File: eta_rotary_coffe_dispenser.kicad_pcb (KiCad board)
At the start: 2 copper layers, 81 x 52 mm, 54 parts, among them J1 Conn_01x08, J3 AVR-ISP-6, J4 Conn_01x02, J5 Conn_01x04, J6 Conn_01x02, J7 Conn_01x02, Q1 IRF640NPbF, Q2 IRF640NPbF, Q3 CPH3350-TL-W, SW1 SW_Push, U1 ATmega328P-A, U2 L7805, Y1 Crystal

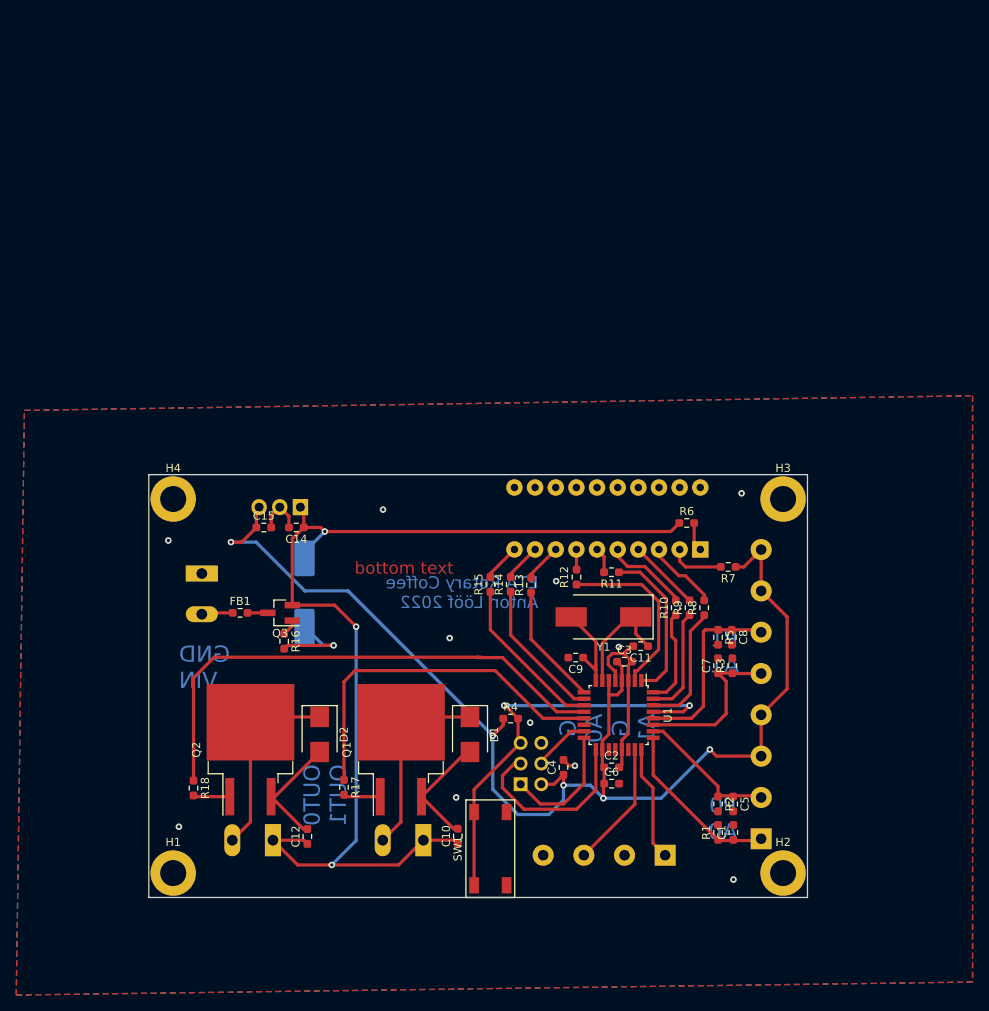
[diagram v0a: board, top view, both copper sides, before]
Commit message: start rev 2 op project with can and weight sens
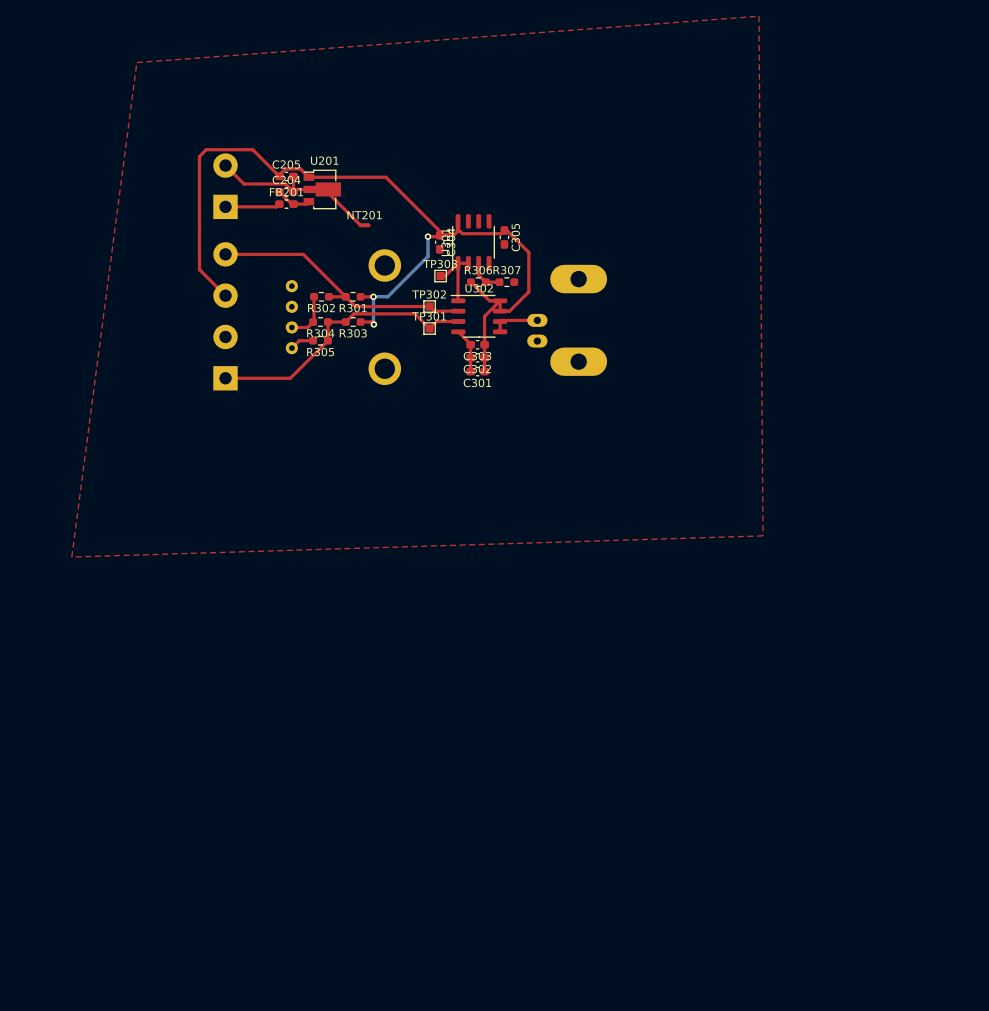
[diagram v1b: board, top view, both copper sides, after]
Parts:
- removed BAR1: HLCP-J100_2, Display:HLCP-J100
- removed C1, C14, C15, C2, C3, C4, C5, C7, C8: 100n, Resistor_SMD:R_0603_1608Metric_Pad0.98x0.95mm_HandSolder
- removed C10, C12, C6: 1u, Resistor_SMD:R_0603_1608Metric_Pad0.98x0.95mm_HandSolder
- removed C11, C9: 12p, Resistor_SMD:R_0603_1608Metric_Pad0.98x0.95mm_HandSolder
- removed C13: 470u, Capacitor_SMD:CP_Elec_10x10.5
- removed D1, D2: SM6T30A, Diode_SMD:D_SMB
- removed FB1: FerriteBead_Small, Resistor_SMD:R_0603_1608Metric_Pad0.98x0.95mm_HandSolder
- removed H1, H2, H3, H4: MountingHole_Pad, MountingHole:MountingHole_3.2mm_M3_DIN965_Pad
- removed J1: Conn_01x08, TerminalBlock_Phoenix:TerminalBlock_Phoenix_MKDS-1,5-8-5.08_1x08_P5.08mm_Horizontal
- removed J3: AVR-ISP-6, Connector_PinHeader_2.54mm:PinHeader_2x03_P2.54mm_Vertical
- removed J4, J6, J7: Conn_01x02, TerminalBlock:TerminalBlock_Altech_AK300-2_P5.00mm
- removed J5: Conn_01x04, TerminalBlock_Phoenix:TerminalBlock_Phoenix_MKDS-1,5-4_1x04_P5.00mm_Horizontal
- removed Q1, Q2: IRF640NPbF, Package_TO_SOT_SMD:TO-263-2
- removed Q3: CPH3350-TL-W, Package_TO_SOT_SMD:SOT-23_Handsoldering
- removed R1, R16, R2, R3, R4, R5: 10k, Resistor_SMD:R_0603_1608Metric_Pad0.98x0.95mm_HandSolder
- removed R10, R11, R12, R13, R14, R15, R17, R18, R7, R8, R9: 470, Resistor_SMD:R_0603_1608Metric_Pad0.98x0.95mm_HandSolder
- removed R6: 4k7, Resistor_SMD:R_0603_1608Metric_Pad0.98x0.95mm_HandSolder
- removed SW1: SW_Push, good_things:push_sw_purple
- removed U1: ATmega328P-A, Package_QFP:TQFP-32_7x7mm_P0.8mm
- removed U2: L7805, Package_TO_SOT_THT:TO-220-3_Vertical
- removed Y1: Crystal, Crystal:Crystal_SMD_EuroQuartz_MQ2-2Pin_7.0x5.0mm_HandSoldering
- added C204: 100n, Capacitor_SMD:C_0603_1608Metric_Pad1.08x0.95mm_HandSolder, F.Cu at (192.8, 57.4)
- added C205: 100n, Capacitor_SMD:C_0603_1608Metric_Pad1.08x0.95mm_HandSolder, F.Cu at (192.8, 55.5)
- added C301: 1u, Capacitor_SMD:C_0603_1608Metric_Pad1.08x0.95mm_HandSolder, F.Cu at (216.3, 79.5)
- added C302: 100n, Capacitor_SMD:C_0603_1608Metric_Pad1.08x0.95mm_HandSolder, F.Cu at (216.3, 77.8)
- added C303: 10n, Capacitor_SMD:C_0603_1608Metric_Pad1.08x0.95mm_HandSolder, F.Cu at (216.3, 76.2)
- added C304: 1u, Capacitor_SMD:C_0603_1608Metric_Pad1.08x0.95mm_HandSolder, F.Cu at (211.7, 63.6)
- added C305: 100n, Capacitor_SMD:C_0603_1608Metric_Pad1.08x0.95mm_HandSolder, F.Cu at (219.6, 63.0)
- added FB201: FerriteBead, Inductor_SMD:L_0603_1608Metric_Pad1.05x0.95mm_HandSolder, F.Cu at (192.8, 58.9)
- added J201: Conn_01x02, TerminalBlock:TerminalBlock_bornier-2_P5.08mm, B.Cu at (185.3, 59.2)
- added J301: Conn_01x04, TerminalBlock:TerminalBlock_bornier-4_P5.08mm, B.Cu at (185.3, 80.3)
- added J302: Conn_Coaxial, Connector_Coaxial:BNC_Amphenol_B6252HB-NPP3G-50_Horizontal, B.Cu at (223.7, 73.2)
- added NT201: NetTie_2, NetTie:NetTie-2_SMD_Pad0.5mm, F.Cu at (202.4, 61.5)
- added R301: 10k, Resistor_SMD:R_0603_1608Metric_Pad0.98x0.95mm_HandSolder, F.Cu at (201.0, 70.3)
- added R302: 10k, Resistor_SMD:R_0603_1608Metric_Pad0.98x0.95mm_HandSolder, F.Cu at (197.1, 70.3)
- added R303: 10k, Resistor_SMD:R_0603_1608Metric_Pad0.98x0.95mm_HandSolder, F.Cu at (201.0, 73.4)
- added R304: 10k, Resistor_SMD:R_0603_1608Metric_Pad0.98x0.95mm_HandSolder, F.Cu at (197.0, 73.4)
- added R305: 82k, Resistor_SMD:R_0603_1608Metric_Pad0.98x0.95mm_HandSolder, F.Cu at (197.0, 75.7)
- added R306: 10k, Resistor_SMD:R_0603_1608Metric_Pad0.98x0.95mm_HandSolder, F.Cu at (216.4, 68.5)
- added R307: 10k, Resistor_SMD:R_0603_1608Metric_Pad0.98x0.95mm_HandSolder, F.Cu at (219.9, 68.5)
- added RV301: 10k, good_things:B10K_POT_ETA, B.Cu at (197.3, 72.8)
- added TP301: TestPoint, TestPoint:TestPoint_Pad_1.0x1.0mm, F.Cu at (210.4, 74.2)
- added TP302: TestPoint, TestPoint:TestPoint_Pad_1.0x1.0mm, F.Cu at (210.4, 71.5)
- added TP303: TestPoint, TestPoint:TestPoint_Pad_1.0x1.0mm, F.Cu at (211.8, 67.8)
- added U201: L78L33_SOT89, Package_TO_SOT_SMD:SOT-89-3, F.Cu at (197.2, 57.1)
- added U301: LM358, Package_SO:SO-8_3.9x4.9mm_P1.27mm, F.Cu at (215.8, 63.6)
- added U302: MAX4196, Package_SO:SO-8_3.9x4.9mm_P1.27mm, F.Cu at (216.5, 72.7)
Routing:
- net VCC: track 155.2 -> 0.00 mm, vias 5 -> 0
- net +12V: track 133.3 -> 0.00 mm, vias 3 -> 0
- net +3.3VA: track 0.00 -> 112.3 mm, vias 0 -> 3
- net /ext_ctrl0: track 65.0 -> 0.00 mm
- net /isp_rst_n: track 53.0 -> 0.00 mm, vias 2 -> 0
- net GND: track 69.1 -> 21.8 mm, vias 12 -> 0
- net /ext_ctrl1: track 44.6 -> 0.00 mm
- net /scale_amp/inp: track 0.00 -> 34.4 mm
- net /scale_amp/inn: track 0.00 -> 33.6 mm
- net /ext_out1: track 24.2 -> 0.00 mm
- net /ext_out0: track 24.2 -> 0.00 mm
- net /rotary1_pulse: track 23.3 -> 0.00 mm
- net /isp_sck: track 22.8 -> 0.00 mm
- net /led_6: track 22.1 -> 0.00 mm
- net /rotary0_active: track 21.3 -> 0.00 mm
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- added copper zone on F.Cu, net GNDA
- removed copper zone on B.Cu, net GND
- removed copper zone on F.Cu, net GND
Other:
- board outline removed
- board text removed: "ETA Rotary Coffee Anton Lööf 2022"
- board text removed: "G A0 G A1"
- board text removed: "GND VIN"
- board text removed: "OUT0 OUT1"
- board text removed: "P0 A0"
- board text removed: "P1 A1"
- board text removed: "bottom text"

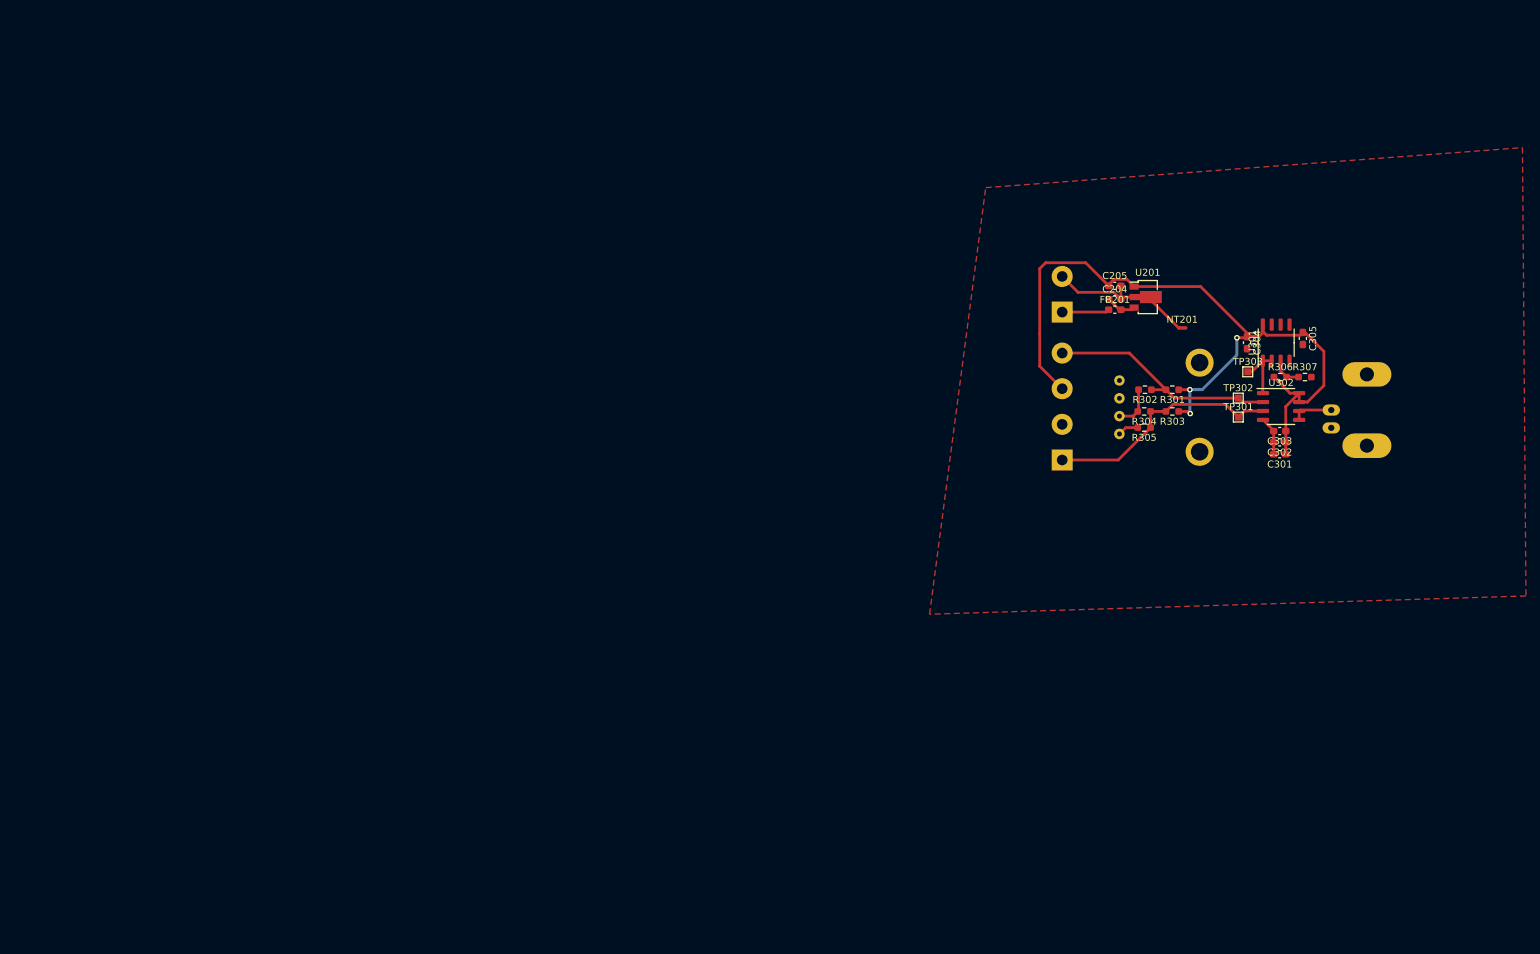
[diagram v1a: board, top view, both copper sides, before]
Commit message: some form of schematic done, still lots to test
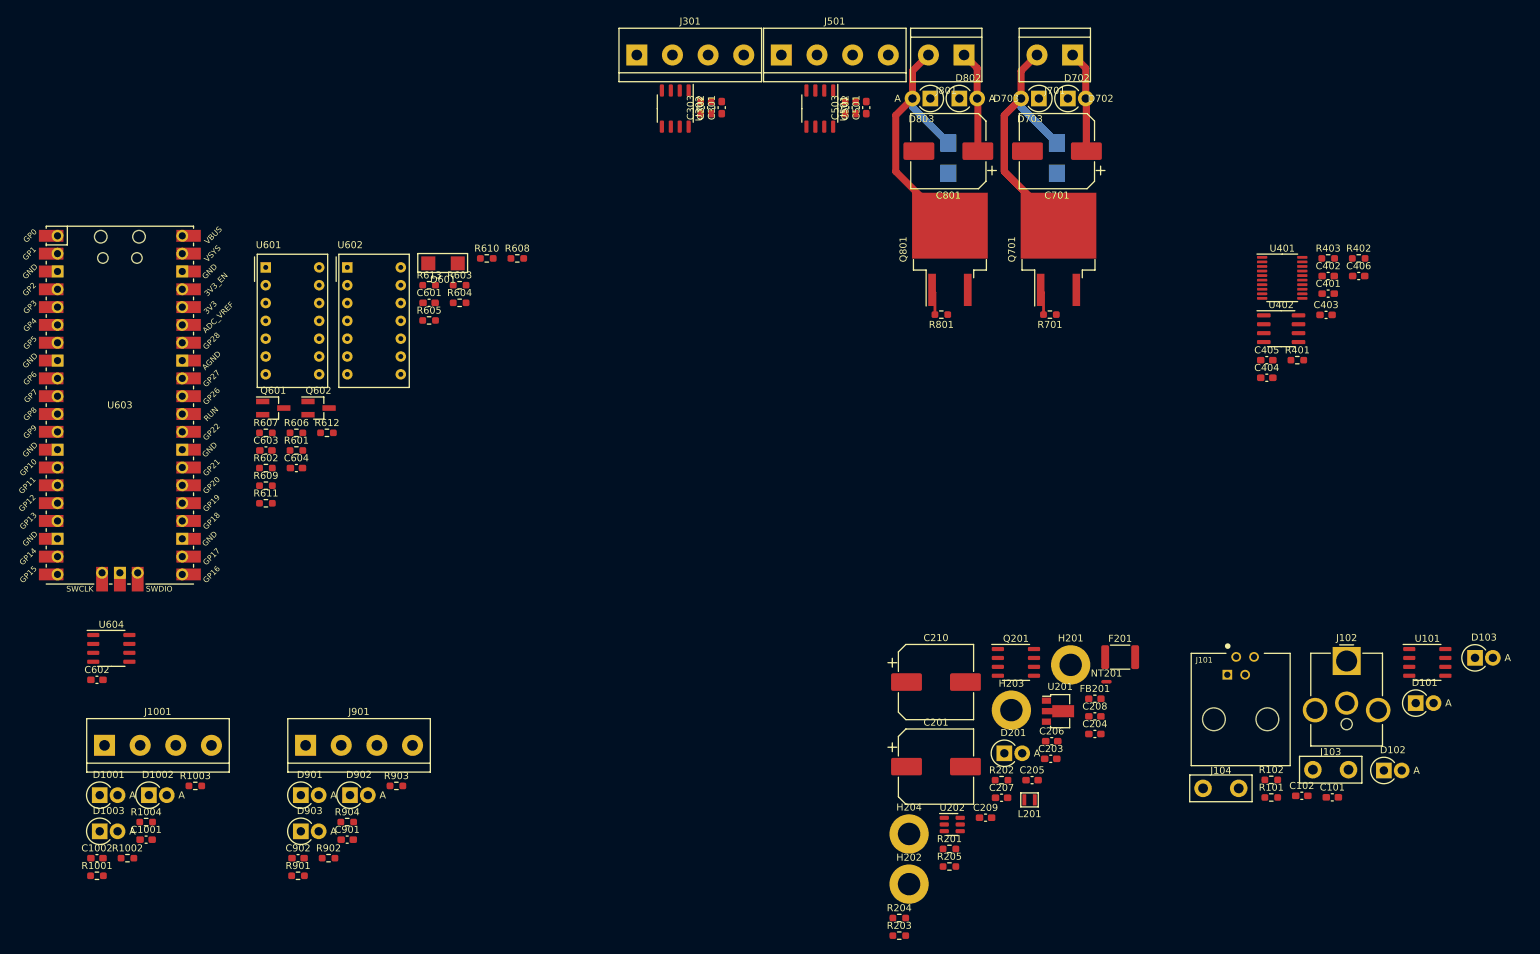
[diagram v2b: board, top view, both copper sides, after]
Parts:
- removed C304: 1u, Capacitor_SMD:C_0603_1608Metric_Pad1.08x0.95mm_HandSolder
- removed C305: 100n, Capacitor_SMD:C_0603_1608Metric_Pad1.08x0.95mm_HandSolder
- removed J201: Conn_01x02, TerminalBlock:TerminalBlock_bornier-2_P5.08mm
- removed J302: Conn_Coaxial, Connector_Coaxial:BNC_Amphenol_B6252HB-NPP3G-50_Horizontal
- removed R301, R302, R303, R304, R306, R307: 10k, Resistor_SMD:R_0603_1608Metric_Pad0.98x0.95mm_HandSolder
- removed R305: 82k, Resistor_SMD:R_0603_1608Metric_Pad0.98x0.95mm_HandSolder
- removed RV301: 10k, good_things:B10K_POT_ETA
- removed TP301, TP302, TP303: TestPoint, TestPoint:TestPoint_Pad_1.0x1.0mm
- removed U301: LM358, Package_SO:SO-8_3.9x4.9mm_P1.27mm
- added C1001: 100n, Capacitor_SMD:C_0603_1608Metric_Pad1.08x0.95mm_HandSolder, F.Cu at (54.7, 134.4)
- added C1002: 100n, Capacitor_SMD:C_0603_1608Metric_Pad1.08x0.95mm_HandSolder, F.Cu at (47.7, 137.1)
- added C101: 1u, Capacitor_SMD:C_0603_1608Metric_Pad1.08x0.95mm_HandSolder, F.Cu at (223.8, 128.4)
- added C102: 100n, Capacitor_SMD:C_0603_1608Metric_Pad1.08x0.95mm_HandSolder, F.Cu at (219.4, 128.2)
- added C201: 470u, Capacitor_SMD:CP_Elec_10x10.5, F.Cu at (167.3, 124.0)
- added C203: 1u 25V, Capacitor_SMD:C_0603_1608Metric_Pad1.08x0.95mm_HandSolder, F.Cu at (183.7, 122.9)
- added C206: 100n, Capacitor_SMD:C_0603_1608Metric_Pad1.08x0.95mm_HandSolder, F.Cu at (183.8, 120.4)
- added C207: dni, Capacitor_SMD:C_0603_1608Metric_Pad1.08x0.95mm_HandSolder, F.Cu at (176.7, 128.5)
- added C208: 22u, Capacitor_SMD:C_0603_1608Metric_Pad1.08x0.95mm_HandSolder, F.Cu at (190.0, 116.9)
- added C209: 22u, Capacitor_SMD:C_0603_1608Metric_Pad1.08x0.95mm_HandSolder, F.Cu at (174.4, 131.3)
- added C210: 470u, Capacitor_SMD:CP_Elec_10x10.5, F.Cu at (167.3, 112.0)
- added C401: 1u, Capacitor_SMD:C_0603_1608Metric_Pad1.08x0.95mm_HandSolder, F.Cu at (223.2, 56.6)
- added C402: 100n, Capacitor_SMD:C_0603_1608Metric_Pad1.08x0.95mm_HandSolder, F.Cu at (223.2, 54.1)
- added C403: 100n, Capacitor_SMD:C_0603_1608Metric_Pad1.08x0.95mm_HandSolder, F.Cu at (222.9, 59.6)
- added C404: 100n, Capacitor_SMD:C_0603_1608Metric_Pad1.08x0.95mm_HandSolder, F.Cu at (214.5, 68.6)
- added C405: 1u, Capacitor_SMD:C_0603_1608Metric_Pad1.08x0.95mm_HandSolder, F.Cu at (214.5, 66.1)
- added C406: 100n, Capacitor_SMD:C_0603_1608Metric_Pad1.08x0.95mm_HandSolder, F.Cu at (227.6, 54.1)
- added C501: 1u, Capacitor_SMD:C_0603_1608Metric_Pad1.08x0.95mm_HandSolder, F.Cu at (157.4, 30.1)
- added C502: 100n, Capacitor_SMD:C_0603_1608Metric_Pad1.08x0.95mm_HandSolder, F.Cu at (155.9, 30.1)
- added C503: 10n, Capacitor_SMD:C_0603_1608Metric_Pad1.08x0.95mm_HandSolder, F.Cu at (154.4, 30.1)
- added C601: 1u, Capacitor_SMD:C_0603_1608Metric_Pad1.08x0.95mm_HandSolder, F.Cu at (95.1, 57.9)
- added C602: 100n, Capacitor_SMD:C_0603_1608Metric_Pad1.08x0.95mm_HandSolder, F.Cu at (47.7, 111.7)
- added C603: 10n, Capacitor_SMD:C_0603_1608Metric_Pad1.08x0.95mm_HandSolder, F.Cu at (71.8, 79.0)
- added C604: 10n, Capacitor_SMD:C_0603_1608Metric_Pad1.08x0.95mm_HandSolder, F.Cu at (76.2, 81.5)
- added C701: 470u, Capacitor_SMD:CP_Elec_10x10.5, F.Cu at (184.6, 36.3)
- added C801: 470u, Capacitor_SMD:CP_Elec_10x10.5, F.Cu at (169.1, 36.3)
- added C901: 100n, Capacitor_SMD:C_0603_1608Metric_Pad1.08x0.95mm_HandSolder, F.Cu at (83.4, 134.4)
- added C902: 100n, Capacitor_SMD:C_0603_1608Metric_Pad1.08x0.95mm_HandSolder, F.Cu at (76.4, 137.1)
- added D1001: P6KE16CA+, Diode_THT:D_DO-15_P2.54mm_Vertical_AnodeUp, F.Cu at (48.1, 128.1)
- added D1002: P6KE16CA+, Diode_THT:D_DO-15_P2.54mm_Vertical_AnodeUp, F.Cu at (55.1, 128.1)
- added D1003: P6KE16CA+, Diode_THT:D_DO-15_P2.54mm_Vertical_AnodeUp, F.Cu at (48.1, 133.2)
- added D101: P6KE16CA+, Diode_THT:D_DO-15_P2.54mm_Vertical_AnodeUp, F.Cu at (235.7, 115.0)
- added D102: P6KE16CA+, Diode_THT:D_DO-15_P2.54mm_Vertical_AnodeUp, F.Cu at (231.2, 124.6)
- added D103: P6KE16CA+, Diode_THT:D_DO-15_P2.54mm_Vertical_AnodeUp, F.Cu at (244.1, 108.5)
- added D201: 5v, Diode_THT:D_DO-15_P2.54mm_Vertical_AnodeUp, F.Cu at (177.1, 122.1)
- added D601: RSX301L-30TE25, good_things:SOD-106, F.Cu at (97.1, 52.3)
- added D701: SM6T30A, Diode_SMD:D_SMB, B.Cu at (184.6, 37.3)
- added D702: P6KE16CA+, Diode_THT:D_DO-15_P2.54mm_Vertical_AnodeUp, F.Cu at (186.1, 28.8)
- added D703: P6KE16CA+, Diode_THT:D_DO-15_P2.54mm_Vertical_AnodeUp, F.Cu at (182.0, 28.8)
- added D801: SM6T30A, Diode_SMD:D_SMB, B.Cu at (169.1, 37.3)
- added D802: P6KE16CA+, Diode_THT:D_DO-15_P2.54mm_Vertical_AnodeUp, F.Cu at (170.6, 28.8)
- added D803: P6KE16CA+, Diode_THT:D_DO-15_P2.54mm_Vertical_AnodeUp, F.Cu at (166.5, 28.8)
- added D901: P6KE16CA+, Diode_THT:D_DO-15_P2.54mm_Vertical_AnodeUp, F.Cu at (76.8, 128.1)
- added D902: P6KE16CA+, Diode_THT:D_DO-15_P2.54mm_Vertical_AnodeUp, F.Cu at (83.8, 128.1)
- added D903: P6KE16CA+, Diode_THT:D_DO-15_P2.54mm_Vertical_AnodeUp, F.Cu at (76.8, 133.2)
- added F201: MC36232, Fuse:Fuse_1812_4532Metric, F.Cu at (193.6, 108.4)
- added H201: MountingHole_Pad, MountingHole:MountingHole_3.2mm_M3_DIN965_Pad, F.Cu at (186.5, 109.5)
- added H202: MountingHole_Pad, MountingHole:MountingHole_3.2mm_M3_DIN965_Pad, F.Cu at (163.5, 140.8)
- added H203: MountingHole_Pad, MountingHole:MountingHole_3.2mm_M3_DIN965_Pad, F.Cu at (178.1, 116.0)
- added H204: MountingHole_Pad, MountingHole:MountingHole_3.2mm_M3_DIN965_Pad, F.Cu at (163.5, 133.6)
- added J1001: Conn_01x04, TerminalBlock:TerminalBlock_bornier-4_P5.08mm, F.Cu at (48.8, 121.0)
- added J101: RJ10, CAN-Distributor:TE_5520257-2, F.Cu at (210.7, 117.3)
- added J102: Barrel_Jack, Connector_BarrelJack:BarrelJack_CUI_PJ-063AH_Horizontal_CircularHoles, F.Cu at (225.8, 109.0)
- added J103: SW, good_things:TE_726386-2, F.Cu at (223.6, 124.5)
- added J104: SW, good_things:TE_726386-2, F.Cu at (207.9, 127.1)
- added J501: Conn_01x04, TerminalBlock:TerminalBlock_bornier-4_P5.08mm, F.Cu at (145.3, 22.6)
- added J701: Conn_01x02, TerminalBlock:TerminalBlock_bornier-2_P5.08mm, F.Cu at (186.8, 22.6)
- added J801: Conn_01x02, TerminalBlock:TerminalBlock_bornier-2_P5.08mm, F.Cu at (171.3, 22.6)
- added J901: Conn_01x04, TerminalBlock:TerminalBlock_bornier-4_P5.08mm, F.Cu at (77.5, 121.0)
- added L201: 2u2, good_things:smd_inductor_0806_2016metric, F.Cu at (180.6, 128.8)
- added Q201: FDS4435, Package_SO:SO-8_3.9x4.9mm_P1.27mm, F.Cu at (178.7, 109.2)
- added Q601: KST5551, Package_TO_SOT_SMD:SOT-23_Handsoldering, F.Cu at (72.9, 72.9)
- added Q602: KST5551, Package_TO_SOT_SMD:SOT-23_Handsoldering, F.Cu at (79.3, 72.9)
- added Q701: IRF640NPbF, Package_TO_SOT_SMD:TO-263-2, F.Cu at (184.8, 50.3)
- added Q801: IRF640NPbF, Package_TO_SOT_SMD:TO-263-2, F.Cu at (169.3, 50.3)
- added R1001: 10k, Resistor_SMD:R_0603_1608Metric_Pad0.98x0.95mm_HandSolder, F.Cu at (47.7, 139.6)
- added R1002: 10k, Resistor_SMD:R_0603_1608Metric_Pad0.98x0.95mm_HandSolder, F.Cu at (52.1, 137.1)
- added R1003: 1k, Resistor_SMD:R_0603_1608Metric_Pad0.98x0.95mm_HandSolder, F.Cu at (61.8, 126.8)
- added R1004: 1k, Resistor_SMD:R_0603_1608Metric_Pad0.98x0.95mm_HandSolder, F.Cu at (54.7, 131.9)
- added R101: 10k, Resistor_SMD:R_0603_1608Metric_Pad0.98x0.95mm_HandSolder, F.Cu at (215.1, 128.4)
- added R102: 10k, Resistor_SMD:R_0603_1608Metric_Pad0.98x0.95mm_HandSolder, F.Cu at (215.1, 125.9)
- added R201: 10k, Resistor_SMD:R_0603_1608Metric_Pad0.98x0.95mm_HandSolder, F.Cu at (169.2, 135.8)
- added R202: 10k, Resistor_SMD:R_0603_1608Metric_Pad0.98x0.95mm_HandSolder, F.Cu at (176.7, 126.0)
- added R203: 2k2, Resistor_SMD:R_0603_1608Metric_Pad0.98x0.95mm_HandSolder, F.Cu at (162.1, 148.1)
- added R204: 52k3, Resistor_SMD:R_0603_1608Metric_Pad0.98x0.95mm_HandSolder, F.Cu at (162.1, 145.6)
- added R205: 10k, Resistor_SMD:R_0603_1608Metric_Pad0.98x0.95mm_HandSolder, F.Cu at (169.2, 138.3)
- added R401: 10k, Resistor_SMD:R_0603_1608Metric_Pad0.98x0.95mm_HandSolder, F.Cu at (218.8, 66.1)
- added R402: 10k, Resistor_SMD:R_0603_1608Metric_Pad0.98x0.95mm_HandSolder, F.Cu at (227.6, 51.6)
- added R403: 10k, Resistor_SMD:R_0603_1608Metric_Pad0.98x0.95mm_HandSolder, F.Cu at (223.2, 51.6)
- added R601: 470, Resistor_SMD:R_0603_1608Metric_Pad0.98x0.95mm_HandSolder, F.Cu at (76.2, 79.0)
- added R602: 470, Resistor_SMD:R_0603_1608Metric_Pad0.98x0.95mm_HandSolder, F.Cu at (71.8, 81.5)
- added R603: 470, Resistor_SMD:R_0603_1608Metric_Pad0.98x0.95mm_HandSolder, F.Cu at (99.4, 55.4)
- added R604: 470, Resistor_SMD:R_0603_1608Metric_Pad0.98x0.95mm_HandSolder, F.Cu at (99.4, 57.9)
- added R605: 470, Resistor_SMD:R_0603_1608Metric_Pad0.98x0.95mm_HandSolder, F.Cu at (95.1, 60.4)
- added R606: 470, Resistor_SMD:R_0603_1608Metric_Pad0.98x0.95mm_HandSolder, F.Cu at (76.2, 76.5)
- added R607: 470, Resistor_SMD:R_0603_1608Metric_Pad0.98x0.95mm_HandSolder, F.Cu at (71.8, 76.5)
- added R608: 470, Resistor_SMD:R_0603_1608Metric_Pad0.98x0.95mm_HandSolder, F.Cu at (107.6, 51.6)
- added R609: 470, Resistor_SMD:R_0603_1608Metric_Pad0.98x0.95mm_HandSolder, F.Cu at (71.8, 84.0)
- added R610: 470, Resistor_SMD:R_0603_1608Metric_Pad0.98x0.95mm_HandSolder, F.Cu at (103.3, 51.6)
- added R611: 470, Resistor_SMD:R_0603_1608Metric_Pad0.98x0.95mm_HandSolder, F.Cu at (71.8, 86.5)
- added R612: 1k, Resistor_SMD:R_0603_1608Metric_Pad0.98x0.95mm_HandSolder, F.Cu at (80.5, 76.5)
- added R613: 10k, Resistor_SMD:R_0603_1608Metric_Pad0.98x0.95mm_HandSolder, F.Cu at (95.1, 55.4)
- added R701: 470, Resistor_SMD:R_0603_1608Metric_Pad0.98x0.95mm_HandSolder, F.Cu at (183.6, 59.6)
- added R801: 470, Resistor_SMD:R_0603_1608Metric_Pad0.98x0.95mm_HandSolder, F.Cu at (168.1, 59.6)
- added R901: 10k, Resistor_SMD:R_0603_1608Metric_Pad0.98x0.95mm_HandSolder, F.Cu at (76.4, 139.6)
- added R902: 10k, Resistor_SMD:R_0603_1608Metric_Pad0.98x0.95mm_HandSolder, F.Cu at (80.7, 137.1)
- added R903: 1k, Resistor_SMD:R_0603_1608Metric_Pad0.98x0.95mm_HandSolder, F.Cu at (90.4, 126.8)
- added R904: 1k, Resistor_SMD:R_0603_1608Metric_Pad0.98x0.95mm_HandSolder, F.Cu at (83.4, 131.9)
- added U101: LM358, Package_SO:SO-8_3.9x4.9mm_P1.27mm, F.Cu at (237.3, 109.2)
- added U202: AP62250, Package_TO_SOT_SMD:TSOT-23-6, F.Cu at (169.6, 132.3)
- added U401: MCP2515-xST, Package_SO:TSSOP-20_4.4x6.5mm_P0.65mm, F.Cu at (216.7, 54.4)
- added U402: MCP2562-E-SN, Package_SO:SOIC-8_3.9x4.9mm_P1.27mm, F.Cu at (216.5, 61.6)
- added U501: MAX4196, Package_SO:SO-8_3.9x4.9mm_P1.27mm, F.Cu at (150.8, 30.2)
- added U601: MAN74A, Display_7Segment:MAN71A, F.Cu at (71.8, 52.9)
- added U602: MAN74A, Display_7Segment:MAN71A, F.Cu at (83.4, 52.9)
- added U603: Pico, MCU_RaspberryPi_and_Boards:RPi_Pico_SMD_TH, F.Cu at (51.0, 72.5)
- added U604: LM358, Package_SO:SO-8_3.9x4.9mm_P1.27mm, F.Cu at (49.8, 107.2)
- J301: moved to F.Cu
- moved U302 96.2 mm to (130.2, 30.2), turned to -90 degrees
- moved C303 94.5 mm to (133.8, 30.1), turned to 90 degrees
- moved C302 94.0 mm to (135.3, 30.1), turned to 90 degrees
- moved C301 93.6 mm to (136.8, 30.1), turned to 90 degrees
- moved J301 83.7 mm to (124.7, 22.6), turned to 0 degrees
- moved C205 71.4 mm to (181.0, 126.0)
- moved C204 62.0 mm to (190.0, 119.4)
- moved U201 60.3 mm to (184.7, 116.1)
- moved FB201 55.5 mm to (190.0, 114.3)
- moved NT201 51.6 mm to (191.6, 111.9)
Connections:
- net /scale_amp/inp renamed /scale_amp/INP
- net /scale_amp/out renamed /ADC0
- J301 pad 2: GNDA -> /scale_amp/INN
- J301 pad 3: +3.3VA -> GNDA
- J301 pad 4: /scale_amp/inn -> +3.3VA
- U302 pad 1: /scale_amp/vref -> /VREF0
- U302 pad 2: /scale_amp/inn -> /scale_amp/INN
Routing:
- net +3.3VA: track 112.3 -> 0.00 mm, vias 3 -> 0
- net /solenoid/EXT_OUT: track 0.00 -> 68.7 mm
- net /motor/EXT_OUT: track 0.00 -> 37.9 mm
- net +12V: track 0.00 -> 36.6 mm
- net /scale_amp/INP: track 34.4 -> 0.00 mm
- net /scale_amp/inn: track 33.6 -> 0.00 mm
- net GND: track 21.8 -> 0.00 mm
- net GNDA: track 11.6 -> 0.00 mm
- net /scale_amp/vref: track 8.70 -> 0.00 mm
- net +5V: track 6.77 -> 0.00 mm
- net /ADC0: track 5.90 -> 0.00 mm
- net /scale_amp/vref_div: track 4.37 -> 0.00 mm
- net /power/3v3a_regin: track 4.36 -> 0.00 mm
- net /motor/EXT_CTRL: track 0.00 -> 3.69 mm
- net /solenoid/EXT_CTRL: track 0.00 -> 3.69 mm
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- removed copper zone on F.Cu, net GNDA
